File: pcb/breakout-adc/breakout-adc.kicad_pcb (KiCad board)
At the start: 4 copper layers, 100 x 62 mm, 104 parts, among them J1 Screw_Terminal_01x04, J10 Conn_01x01_Pin, J11 Conn_01x12_Pin, J12 Conn_01x12_Pin, J13 Conn_01x01_Pin, J14 Conn_01x01_Pin, J15 FX18-120P-0.8SV20, J2 Screw_Terminal_01x02, J20 Conn_02x02_Counter_Clockwise, J21 Conn_02x04_Odd_Even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

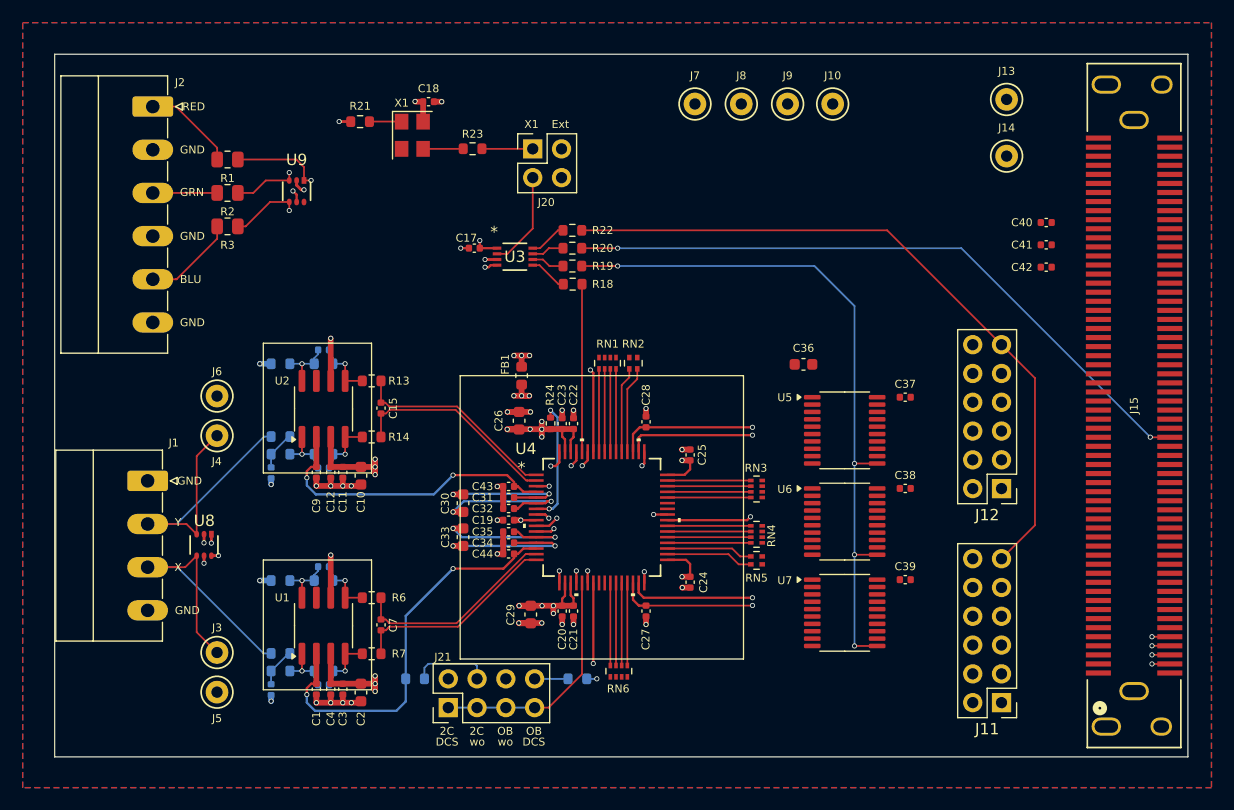
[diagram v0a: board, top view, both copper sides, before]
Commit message: [adc][pcb] flip flop inputs routed
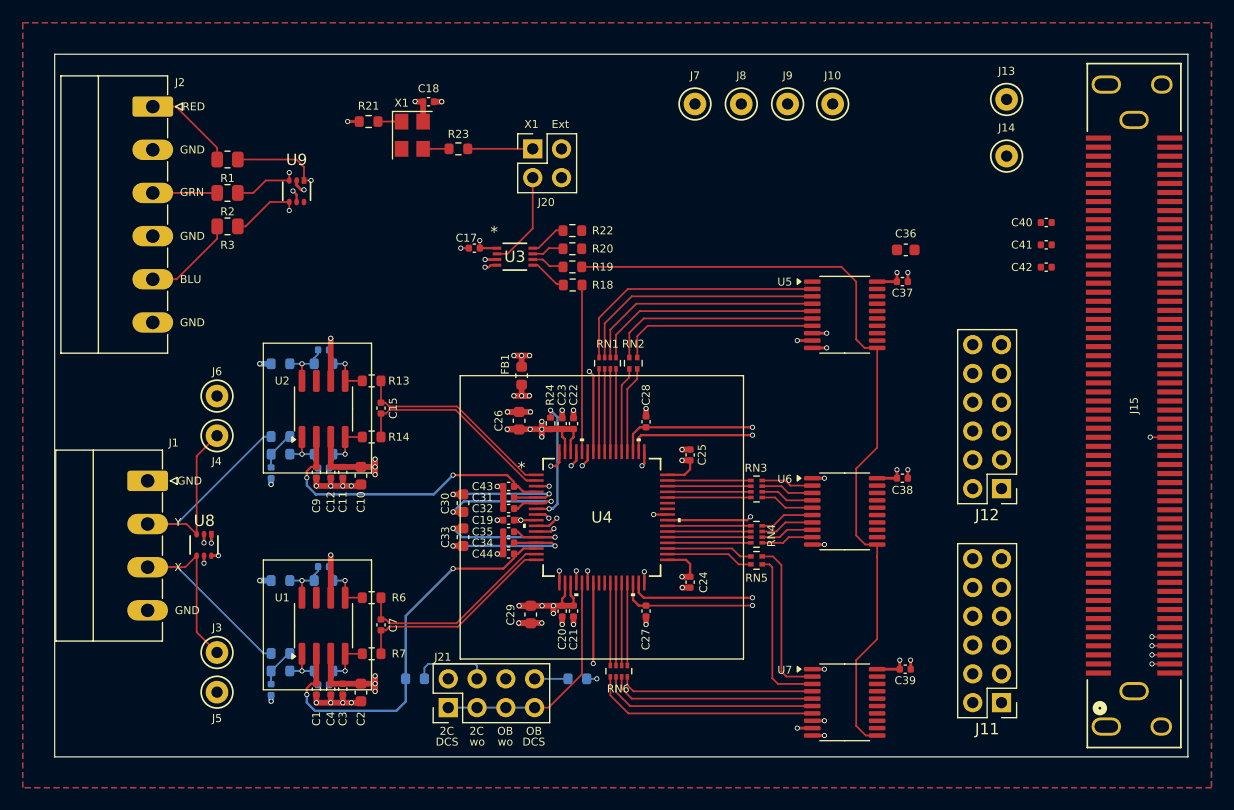
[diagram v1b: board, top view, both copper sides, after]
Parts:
- moved C36 13.5 mm to (183.8, 60.8)
- moved C37 10.2 mm to (183.5, 63.6)
- moved U5 10.2 mm to (178.4, 66.5)
- moved C39 7.90 mm to (183.7, 97.8)
- moved U7 7.90 mm to (178.4, 100.7)
- moved R23 1.25 mm to (144.3, 51.9)
- moved C38 0.93 mm to (183.5, 81.0)
- moved U6 0.90 mm to (178.4, 83.9)
- moved R21 0.75 mm to (136.4, 49.5)
- moved R18 0.07 mm to (154.4, 63.9)
- moved R19 0.07 mm to (154.4, 62.3)
- moved R20 0.05 mm to (154.4, 60.7)
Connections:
- U5 pad 8: /adc/DB3 -> GND
- U5 pad 9: /adc/DB2 -> GND
- U6 pad 2: /adc/DB1 -> /adc/DB3
- U6 pad 3: /adc/DB0 -> /adc/DB2
- U6 pad 4: /adc/DA9 -> /adc/DB1
- U6 pad 5: /adc/DA8 -> /adc/DB0
- U6 pad 6: /adc/DA7 -> /adc/DA9
- U6 pad 7: /adc/DA6 -> /adc/DA8
- U6 pad 8: /adc/DA5 -> /adc/DA7
- U6 pad 9: /adc/DA4 -> /adc/DA6
- U7 pad 2: /adc/DA3 -> /adc/DA5
- U7 pad 3: /adc/DA2 -> /adc/DA4
- U7 pad 4: /adc/DA1 -> /adc/DA3
- U7 pad 5: /adc/DA0 -> /adc/DA2
- U7 pad 6: GND -> /adc/DA1
- U7 pad 7: GND -> /adc/DA0
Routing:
- net /ADC_CLK_HDR: track 62.6 -> 0.00 mm
- net /ADC_CLK_FPGA: track 58.8 -> 1.73 mm, vias 2 -> 1
- net /adc/DB9: track 0.00 -> 23.4 mm
- net /adc/DB8: track 0.00 -> 22.3 mm
- net /adc/DB7: track 0.00 -> 21.2 mm
- net /adc/DB6: track 0.00 -> 20.2 mm
- net /adc/DA0: track 0.00 -> 20.1 mm
- net /adc/DA1: track 0.00 -> 19.2 mm
- net /adc/DB5: track 0.00 -> 18.9 mm
- net /adc/DA2: track 0.00 -> 18.2 mm
- net /adc/DB4: track 0.00 -> 17.7 mm
- net /adc/DA3: track 0.00 -> 17.3 mm
- net /adc/DA4: track 0.00 -> 14.5 mm
- net /adc/DA5: track 0.00 -> 14.3 mm
- net GND: track 110.5 -> 123.4 mm, vias 56 -> 68
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
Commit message: [adc][pcb] improve ergonomics of test points
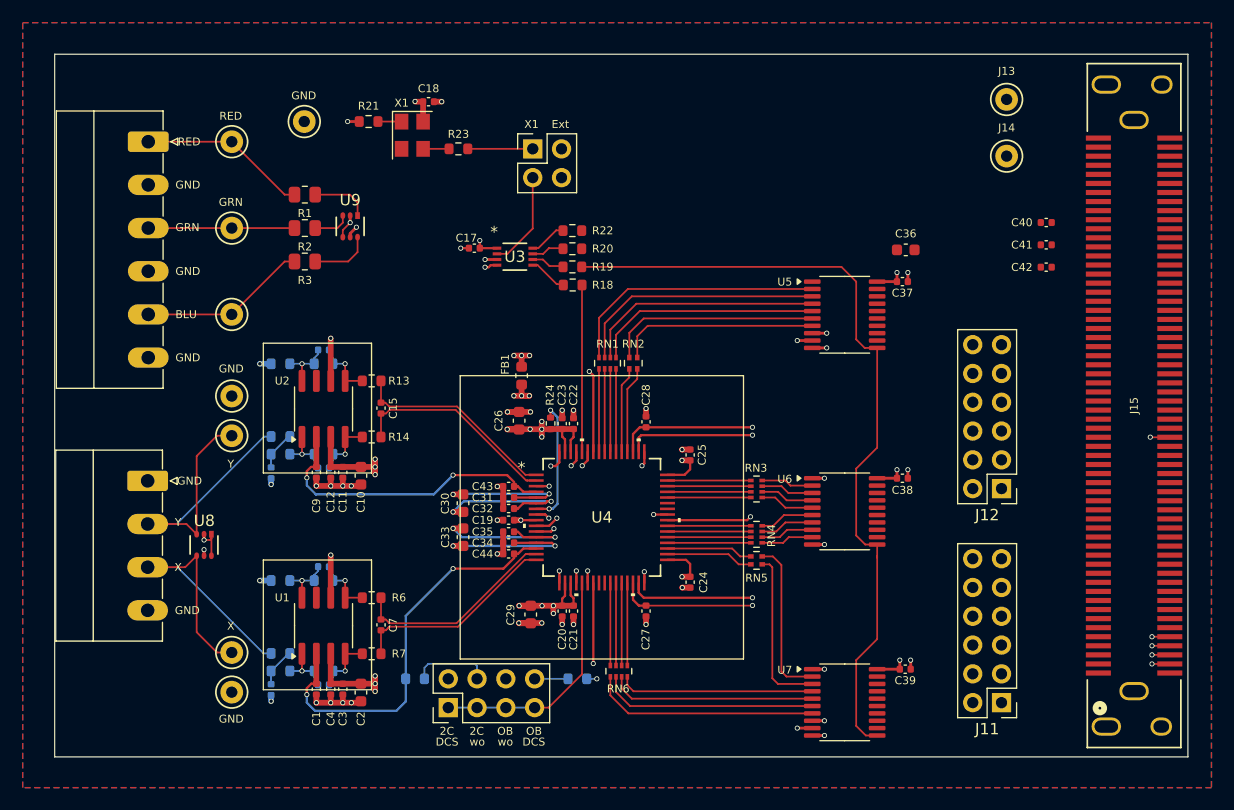
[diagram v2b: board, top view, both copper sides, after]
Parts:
- moved J9 52.4 mm to (124.3, 66.5)
- moved J10 46.7 mm to (130.7, 49.5)
- moved J8 46.3 mm to (124.3, 58.9)
- moved J7 41.0 mm to (124.3, 51.3)
- moved R2 7.50 mm to (130.8, 58.9)
- moved R3 7.50 mm to (130.8, 61.8)
- moved R1 7.50 mm to (130.8, 55.9)
- moved U9 5.65 mm to (134.8, 58.7)
- moved J2 3.13 mm to (116.9, 51.3)
- moved J3 1.30 mm to (124.3, 96.3)
- moved J4 1.30 mm to (124.3, 77.2)
- moved J5 1.30 mm to (124.3, 99.8)
- moved J6 1.30 mm to (124.3, 73.7)
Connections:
- J2 pad 1: Net-(J2-Pin_1) -> /RED_IN
- J2 pad 3: Net-(J2-Pin_3) -> /GRN_IN
- J2 pad 5: Net-(J2-Pin_5) -> /BLU_IN
- J7 pad 1: /R -> /RED_IN
- J8 pad 1: /G -> /GRN_IN
- J9 pad 1: /B -> /BLU_IN
- R1 pad 2: Net-(J2-Pin_1) -> /RED_IN
- R2 pad 2: Net-(J2-Pin_3) -> /GRN_IN
- R3 pad 2: Net-(J2-Pin_5) -> /BLU_IN
- U9 pad 4: /B -> GND
- U9 pad 6: GND -> /B
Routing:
- net /BLU_IN: track 0.00 -> 14.8 mm
- net /RED_IN: track 0.00 -> 14.8 mm
- net /GRN_IN: track 0.00 -> 12.9 mm
- net Net-(J2-Pin_5): track 8.25 -> 0.00 mm
- net Net-(J2-Pin_1): track 8.22 -> 0.00 mm
- net Net-(J2-Pin_3): track 5.68 -> 0.00 mm
- net /R: track 7.92 -> 5.19 mm, vias 1 -> 0
- net /G: track 5.69 -> 3.26 mm, vias 1 -> 0
- net GND: track 123.4 -> 125.7 mm, vias 68 -> 66
- net /Y: track 28.2 -> 29.5 mm
- net /X: track 28.1 -> 29.4 mm
- net /B: track 6.18 -> 5.40 mm, vias 1 -> 0

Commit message: [adc][pcb] add more gnd test points
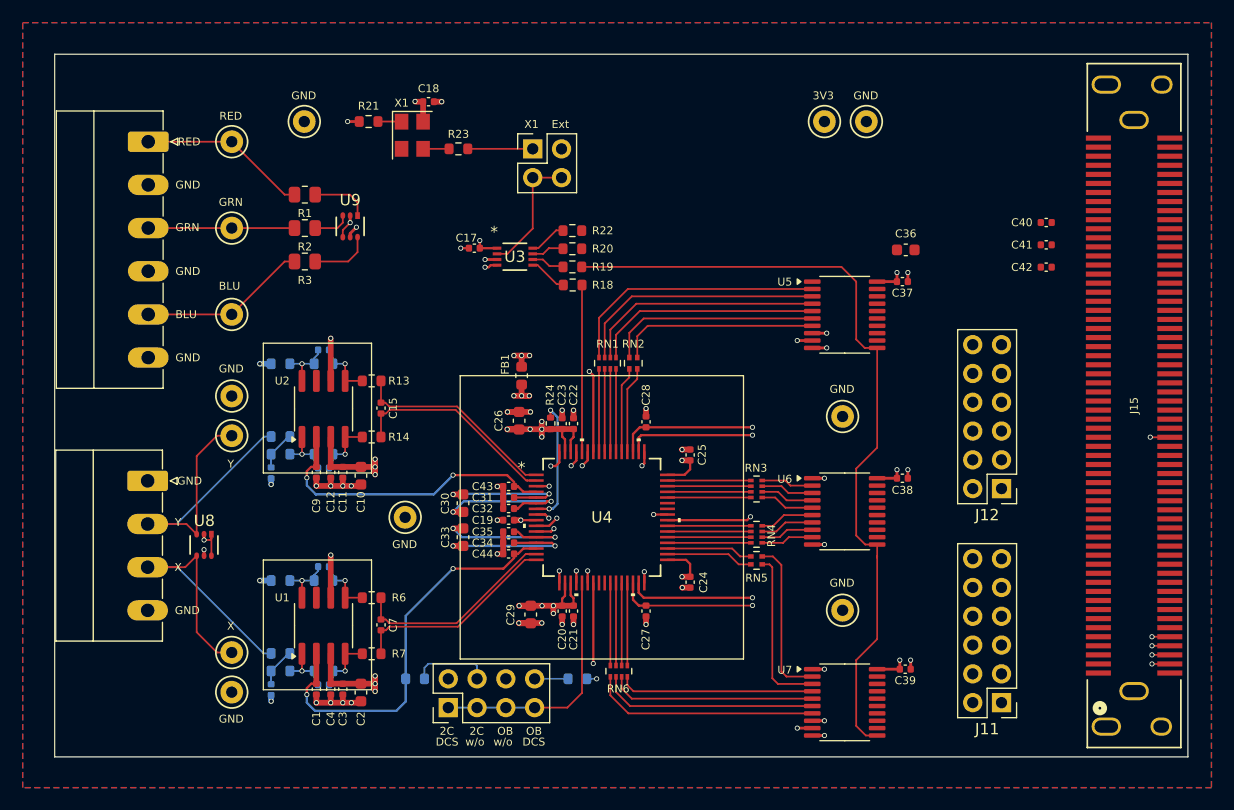
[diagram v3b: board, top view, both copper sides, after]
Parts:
- added J16: Conn_01x01_Pin, TestPoint:TestPoint_Keystone_5000-5004_Miniature, F.Cu at (178.2, 75.5)
- added J17: Conn_01x01_Pin, TestPoint:TestPoint_Keystone_5000-5004_Miniature, F.Cu at (178.2, 92.6)
- added J18: Conn_01x01_Pin, TestPoint:TestPoint_Keystone_5000-5004_Miniature, F.Cu at (139.6, 84.4)
- moved J13 16.2 mm to (176.6, 49.5)
- moved J14 12.7 mm to (180.3, 49.5)
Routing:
- net Net-(J20-Pin_3): track 8.57 -> 11.1 mm
- net Net-(J21-Pin_1): track 21.1 -> 22.0 mm
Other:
- board text added: "3V3"
- board text added: "w/o"
- board text removed: "wo"

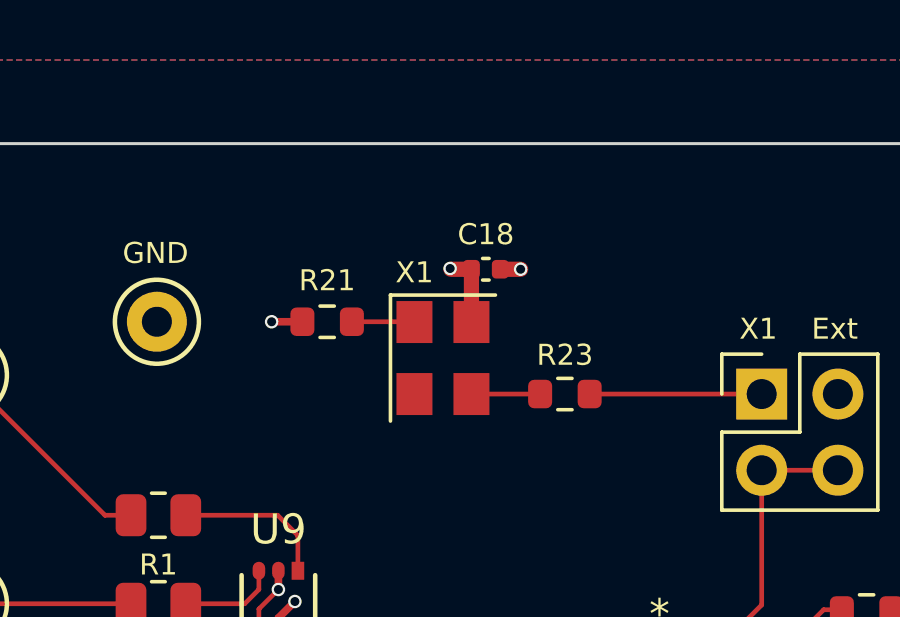
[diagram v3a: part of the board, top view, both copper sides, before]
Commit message: [adc][pcb] oscillator pwr touch ups
give a bit more space to solder the cap, and
add a gnd via nearby the gnd pin
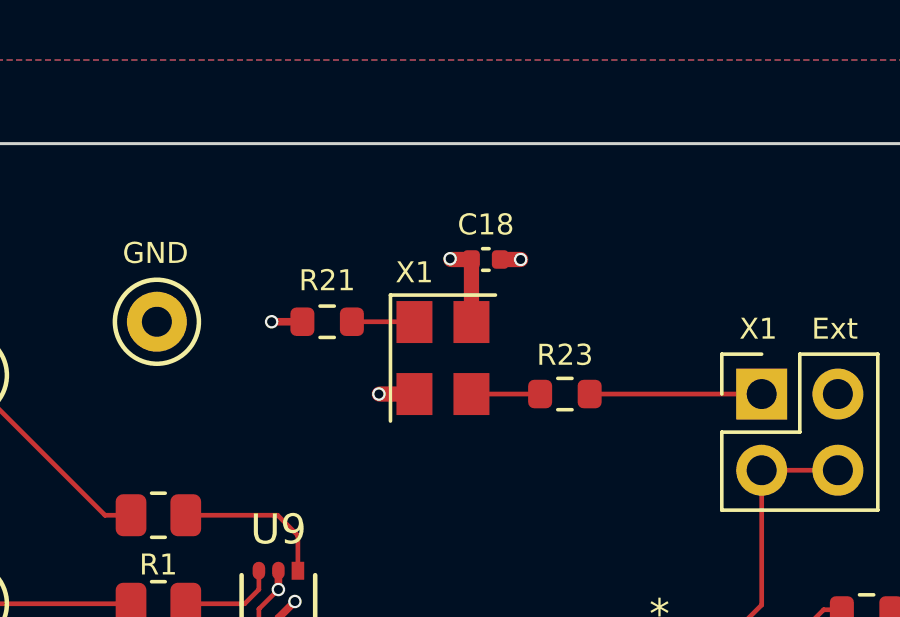
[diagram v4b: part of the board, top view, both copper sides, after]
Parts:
- moved C18 0.33 mm to (141.7, 47.4)
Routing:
- net GND: track 125.7 -> 126.9 mm, vias 66 -> 67
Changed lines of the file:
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@@
 	(footprint "Capacitor_SMD:C_0402_1005Metric"
 		(layer "F.Cu")
-		(at 141.665 47.725)
+		(at 141.665 47.4)
 		(descr "Capacitor SMD 0402 (1005 Metric), square (rectangular) end terminal, IPC_7351 nominal, (Body size source: IPC-SM-782 page 76, https://www.pcb-3d.com/wordpress/wp-content/uploads/ipc-sm-782a_amendment_1_and_2.pdf), generated with kicad-footprint-generator")
 		(tags "capacitor")
@@
 	)
 	(segment
+		(start 139.285 51.884999)
+		(end 138.115001 51.884999)
+		(width 0.508)
+		(layer "F.Cu")
+		(net 1)
+	)
+	(segment
 		(start 147.731666 87.625)
 		(end 148.251666 87.625)
@@
 	)
 	(segment
-		(start 142.145 47.725)
-		(end 142.825 47.725)
+		(start 142.145 47.4)
+		(end 142.825 47.4)
 		(width 0.508)
 		(layer "F.Cu")
@@
 	)
 	(via
-		(at 142.825 47.725)
+		(at 142.825 47.4)
 		(size 0.45)
 		(drill 0.3)
@@
 	)
 	(via
+		(at 138.1 51.884999)
+		(size 0.45)
+		(drill 0.3)
+		(layers "F.Cu" "B.Cu")
+		(net 1)
+	)
+	(via
 		(at 133.035 68.6)
 		(size 0.45)
@@
 	)
 	(segment
+		(start 141.185 47.4)
+		(end 141.185 49.484998)
+		(width 0.508)
+		(layer "F.Cu")
+		(net 3)
+	)
+	(segment
 		(start 146.186866 60.649999)
 		(end 146.186866 59.988134)
@@
 	)
 	(segment
-		(start 140.5 47.725)
-		(end 140.475 47.7)
+		(start 140.5 47.4)
+		(end 140.475 47.375)
 		(width 0.254)
 		(layer "F.Cu")
@@
 	)
 	(segment
-		(start 141.185 47.725)
-		(end 141.185 49.484998)
-		(width 0.508)
-		(layer "F.Cu")
-		(net 3)
-	)
-	(segment
 		(start 160.856666 76.455)
 		(end 170.245 76.455)
@@
 	)
 	(segment
-		(start 141.185 47.725)
-		(end 140.5 47.725)
+		(start 141.185 47.4)
+		(end 140.5 47.4)
 		(width 0.508)
 		(layer "F.Cu")
@@
 	)
 	(via
-		(at 140.475 47.7)
+		(at 140.475 47.375)
 		(size 0.45)
 		(drill 0.3)

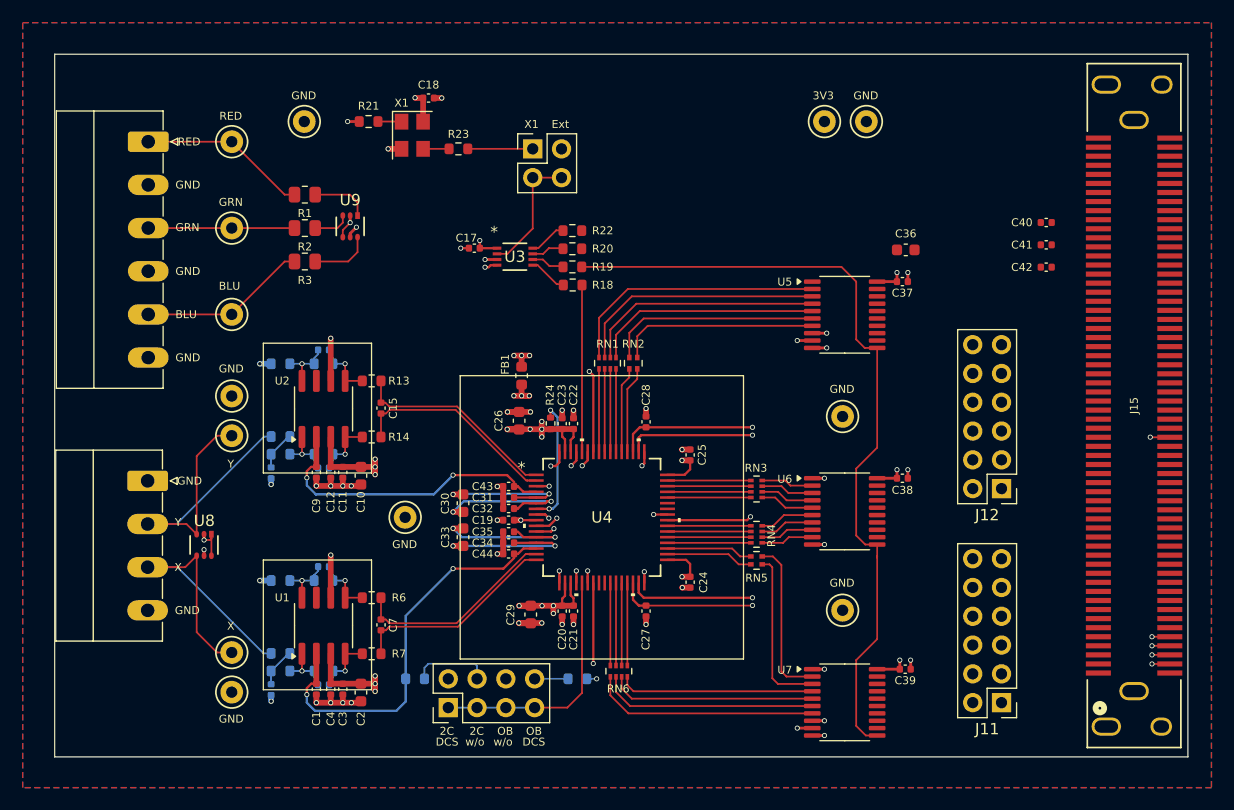
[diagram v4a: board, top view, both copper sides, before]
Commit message: [adc][pcb] add colored keystone tp fp and models
Note: these need to have their footprints and models fixed
as they get used. I only did the ones on this board, even
though I downloaded and committed all the colors.
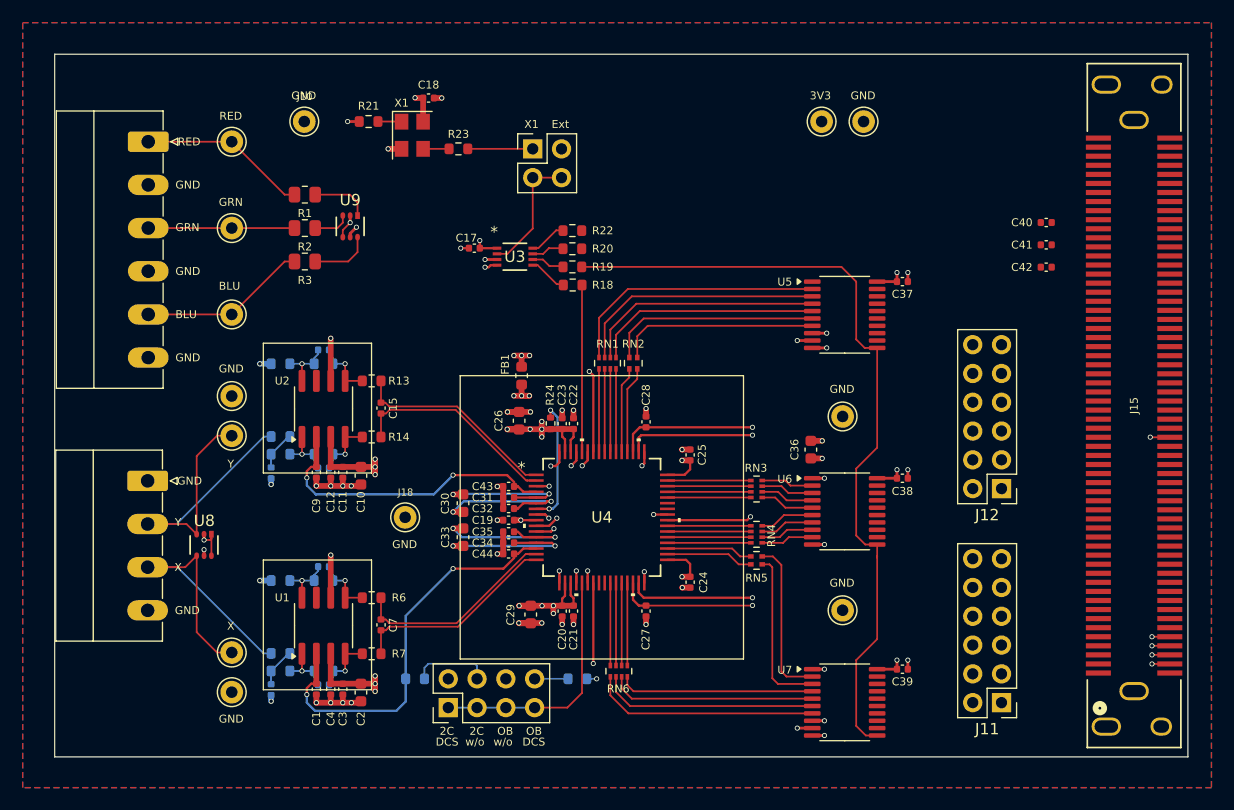
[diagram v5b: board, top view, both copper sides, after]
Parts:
- J10, J14, J16, J17, J18, J5, J6: footprint TestPoint:TestPoint_Keystone_5000-5004_Miniature -> keystone:KEYSTONE_5001
- J13, J7: footprint TestPoint:TestPoint_Keystone_5000-5004_Miniature -> keystone:KEYSTONE_5000
- J3, J4: footprint TestPoint:TestPoint_Keystone_5000-5004_Miniature -> keystone:KEYSTONE_5002
- J8: footprint TestPoint:TestPoint_Keystone_5000-5004_Miniature -> keystone:KEYSTONE_5116
- J9: footprint TestPoint:TestPoint_Keystone_5000-5004_Miniature -> keystone:KEYSTONE_5117
- moved C36 19.5 mm to (175.4, 78.4), turned to 90 degrees
- moved C39 0.25 mm to (183.5, 97.8)
- moved J13 0.25 mm to (176.3, 49.5)
- moved J14 0.25 mm to (180.1, 49.5)
- turned J3 to 0 degrees
- turned J4 to 0 degrees
- turned J5 to 0 degrees
- turned J6 to 0 degrees
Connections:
- J3 pad 1: /X -> (no net)
- J4 pad 1: /Y -> (no net)
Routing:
- net GND: track 126.9 -> 127.9 mm, vias 67 -> 68
- net +3V3: track 42.0 -> 42.6 mm, vias 12 -> 13
